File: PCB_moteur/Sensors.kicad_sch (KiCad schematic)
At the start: 9 parts, among them J4 Conn_01x04_Socket, J6 Conn_01x04_Socket, U10 INA333xxDGK, U11 MAX6612MXK, U5 INA125UA/2K5, U6 INA125UA/2K5

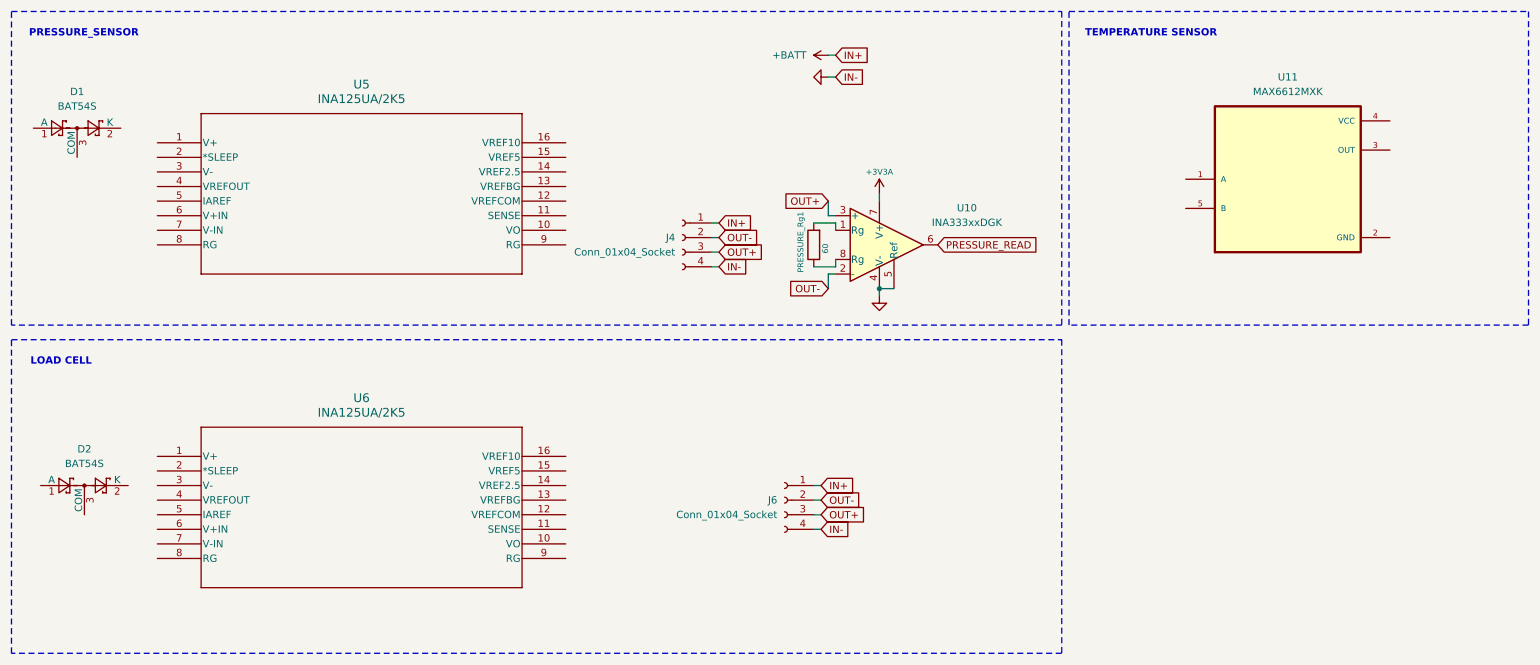
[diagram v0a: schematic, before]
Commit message: finis pression, loadcell, temperature
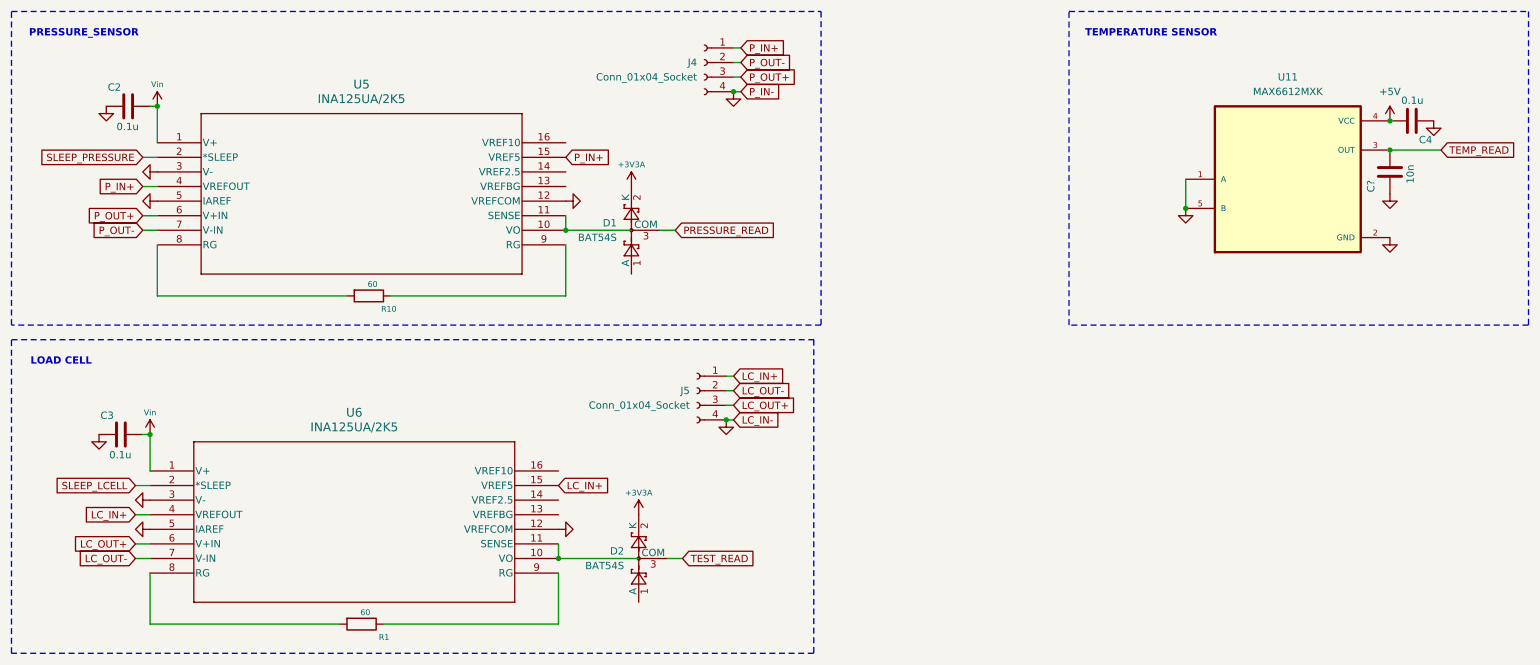
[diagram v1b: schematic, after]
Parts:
- removed J6: Conn_01x04_Socket, symbol Connector:Conn_01x04_Socket
- removed PRESSURE_Rg1: 60, Resistor_SMD:R_0805_2012Metric, symbol Device:R
- removed U10: INA333xxDGK, Package_SO:VSSOP-8_3x3mm_P0.65mm, symbol Amplifier_Instrumentation:INA333xxDGK
- added C2, C3, C4: 0.1u, symbol Device:C
- added C?: 10n, symbol Device:C
- added J5: Conn_01x04_Socket, symbol Connector:Conn_01x04_Socket
- added R1, R10: 60, Resistor_SMD:R_0805_2012Metric, symbol Device:R
- U11: DigiKey_Part_Number (none) -> MAX6612MXK+TCT-ND; Manufacturer_Part_Number (none) -> MAX6612MXK+T
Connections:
- net +BATT is gone; now on net P_IN+: J4.1 (Pin_1)
- net OUT+ is gone; now on net P_OUT+: J4.3 (Pin_3)
- net OUT- is gone; now on net P_OUT-: J4.2 (Pin_2)
- net +3V3A: now also D1.2 (K), D2.2 (K)
- net GND: now also U11.1 (A), U11.2 (GND), U11.5 (B), U5.12 (VREFCOM), U5.3 (V-), U5.5 (IAREF), U6.12 (VREFCOM), U6.3 (V-), U6.5 (IAREF), C2.2, C3.2, C4.2, C?.2, J5.4 (Pin_4)
- net PRESSURE_READ: now also D1.3 (COM)
- net TEST_READ: now reaches D2.3 (COM)
- net Vin: now reaches U6.1 (V+)
- net Vin: now also U5.1 (V+), C2.1, C3.1
- net at U6.10 (VO): now also U6.11 (SENSE)
- net LC_IN+: now reaches U6.15 (VREF5)
- net LC_IN+: now also U6.4 (VREFOUT), J5.1 (Pin_1)
- net SLEEP_LCELL: now reaches U6.2 (*SLEEP)
- net LC_OUT+: now reaches U6.6 (V+IN)
- net LC_OUT+: now also J5.3 (Pin_3)
- net LC_OUT-: now reaches U6.7 (V-IN)
- net LC_OUT-: now also J5.2 (Pin_2)
- net at U6.8 (RG): now also R1.2
- net at U6.9 (RG): now also R1.1
- net TEMP_READ: now reaches U11.3 (OUT)
- net TEMP_READ: now also C?.1
- net +5V: now reaches U11.4 (VCC)
- net +5V: now also C4.1
- net at U5.10 (VO): now also U5.11 (SENSE)
- net P_IN+: now reaches U5.15 (VREF5)
- net P_IN+: now also U5.4 (VREFOUT)
- net SLEEP_PRESSURE: now reaches U5.2 (*SLEEP)
- net P_OUT+: now reaches U5.6 (V+IN)
- net P_OUT-: now reaches U5.7 (V-IN)
- net at U5.8 (RG): now also R10.2
- net at U5.9 (RG): now also R10.1
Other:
- moved on the sheet: D1, J4

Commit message: fix: pyros resistors + typos +
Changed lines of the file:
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@@
+	(wire
+		(pts
+			(xy 222.25 50.8) (xy 222.25 49.53)
+		)
+		(stroke
+			(width 0)
+			(type default)
+		)
+	)
 	(wire
 		(pts
@@
 	(symbol
 		(lib_id "power:GND")
-		(at 222.25 49.53 0)
+		(at 222.25 50.8 0)
 		(unit 1)
 		(exclude_from_sim no)
@@
 		(fields_autoplaced yes)
 		(property "Reference" "#PWR079"
+			(at 222.25 57.15 0)
+			(effects
+				(font
+					(size 1 1)
+				)
+				(hide yes)
+			)
+		)
+		(property "Value" "GND"
 			(at 222.25 55.88 0)
 			(effects
@@
 			)
 		)
-		(property "Value" "GND"
-			(at 222.25 54.61 0)
-			(effects
-				(font
-					(size 1 1)
-				)
-				(hide yes)
-			)
-		)
 		(property "Footprint" ""
-			(at 222.25 49.53 0)
+			(at 222.25 50.8 0)
 			(effects
 				(font
@@
 		)
 		(property "Datasheet" ""
-			(at 222.25 49.53 0)
+			(at 222.25 50.8 0)
 			(effects
 				(font
@@
 		)
 		(property "Description" ""
-			(at 222.25 49.53 0)
-			(effects
-				(font
+			(at 222.25 50.8 0)
+			(effects
+				(font

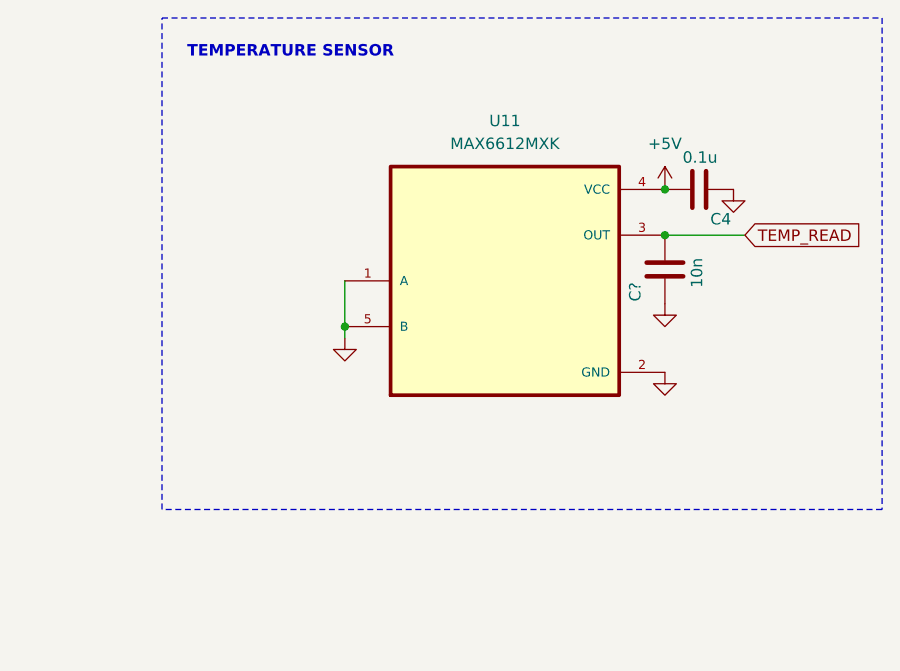
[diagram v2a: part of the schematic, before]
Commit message: fix: resistance ratios + typos
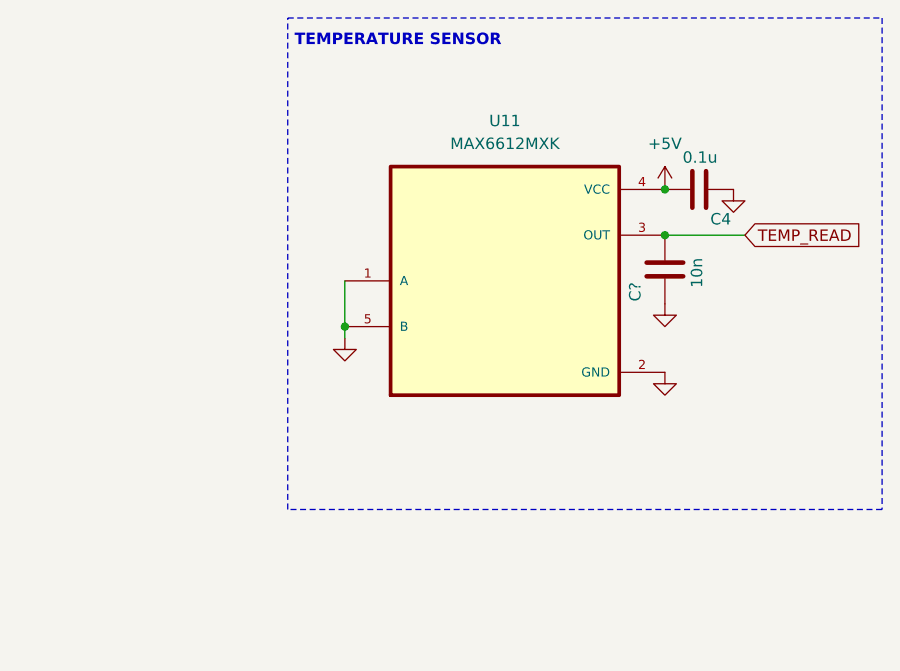
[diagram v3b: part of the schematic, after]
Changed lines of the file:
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@@
 	(paper "A4")
 	(rectangle
-		(start 201.93 15.24)
+		(start 215.9 15.24)
 		(end 281.94 69.85)
 		(stroke
@@
 	(text "TEMPERATURE SENSOR"
 		(exclude_from_sim no)
-		(at 204.724 19.812 0)
+		(at 216.662 18.542 0)
 		(effects
 			(font
